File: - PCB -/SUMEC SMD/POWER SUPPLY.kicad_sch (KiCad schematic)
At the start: 14 parts, among them Q3 PMOS, U10 TB6612FNG, U11 LM1084-3.3

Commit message: pcb update cleanup
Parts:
- C?: footprint Connector_JST:JST_SHL_SM06B-SHLS-TF_1x06-1MP_P1.00mm_Horizontal -> Capacitor_SMD:C_1206_3216Metric
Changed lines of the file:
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@@
       (effects (font (size 1.27 1.27)) (justify left))
     )
-    (property "Footprint" "Connector_JST:JST_SHL_SM06B-SHLS-TF_1x06-1MP_P1.00mm_Horizontal" (at 132.3848 119.38 0)
+    (property "Footprint" "Capacitor_SMD:C_1206_3216Metric" (at 132.3848 119.38 0)
       (effects (font (size 1.27 1.27)) hide)
     )

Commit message: pcb schematic update
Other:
- note added: "EXPLANATION"
- note added: "Voltage regulator - 3,3V Output current - 5A"
- note added: "XT-30 Connector (male) Connector with 2mm bullets contacts for currents up to 30 A. Gold-plated contacts Non-interchangeable polarity. connected with XT-30 female type connector that is wired to the battery Battery specs: - 2S LiPo - 3.7V nominal voltage on one cell - 8,4 in total (4,2 fully charged) - 400mAh 1 Bought and 1 Home-made (Terrorist-like)"
- note removed: "XT-30 Connector (male) Connector with 2mm bullets contacts for currents up to 30 A. Gold-plated contacts Non-interchangeable polarity. connected with XT-30 female type connector that is wired to the battery Battery specs: - 3S LiPo - 3.7V nominal voltage on one cell - 12,6 in total (4,2 fully charged) - 400mAh 1 Bought and 1 Home-made (Terrorist-like)"
- note removed: "https://electronics.stackexchange.com/questions/510248/does-tb6612fng-require-additional-circuit-to-control-motor-and-why"
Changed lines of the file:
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@@
     (effects (font (size 1.3 1.3) italic) (justify left bottom))
+  )
+  (text "Voltage regulator - 3,3V\nOutput current - 5A" (at 22.86 100.33 0)
+    (effects (font (size 1.27 1.27)) (justify left bottom))
   )
   (text "H-MŮSTEK" (at 158.75 17.78 0)
     (effects (font (size 1.5 1.5)) (justify left bottom))
   )
-  (text "XT-30 Connector (male)\n\nConnector with 2mm bullets contacts for currents up to 30 A.\nGold-plated contacts\nNon-interchangeable polarity.\nconnected with XT-30 female type connector that is wired to the battery\n\nBattery specs:\n- 3S LiPo\n- 3.7V nominal voltage on one cell\n- 12,6 in total (4,2 fully charged)\n- 400mAh \n\n1 Bought and 1 Home-made (Terrorist-like)"
+  (text "XT-30 Connector (male)\n\nConnector with 2mm bullets contacts for currents up to 30 A.\nGold-plated contacts\nNon-interchangeable polarity.\nconnected with XT-30 female type connector that is wired to the battery\n\nBattery specs:\n- 2S LiPo\n- 3.7V nominal voltage on one cell\n- 8,4 in total (4,2 fully charged)\n- 400mAh \n\n1 Bought and 1 Home-made (Terrorist-like)"
     (at 20.32 177.8 0)
     (effects (font (size 1.27 1.27) italic) (justify left bottom))
@@
   )
   (text "není toho hodně? mohli bysme to ulehčit." (at 199.39 25.4 0)
-    (effects (font (size 2 2)) (justify left bottom))
+    (effects (font (size 2 2) (color 255 0 0 1)) (justify left bottom))
   )
-  (text "https://electronics.stackexchange.com/questions/510248/does-tb6612fng-require-additional-circuit-to-control-motor-and-why"
-    (at 180.34 16.51 0)
-    (effects (font (size 1 1)) (justify left bottom))
+  (text "EXPLANATION" (at 223.52 80.01 0)
+    (effects (font (face "Arial Unicode MS") (size 2 2)) (justify left bottom) (href "https://electronics.stackexchange.com/questions/510248/does-tb6612fng-require-additional-circuit-to-control-motor-and-why"))
   )
   (text "XT30M KONEKTOR" (at 54.61 146.05 0)

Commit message: PCB cooler schematic and start of board making
bettr cal sol
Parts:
- removed C18: 10uF, Capacitor_SMD:C_1206_3216Metric, symbol Device:C_Polarized
- removed C19: 1uF, Capacitor_SMD:C_1206_3216Metric, symbol Device:C_Polarized
- removed C?: 0,1uF, Capacitor_SMD:C_1206_3216Metric, symbol Device:C
- removed C?: 0,5uF, Capacitor_SMD:C_1206_3216Metric, symbol Device:C
- removed C?: 10uF, Capacitor_SMD:C_1206_3216Metric, symbol Device:C
- removed D7: D_Zener, Diode_SMD:D_1206_3216Metric, symbol Device:D_Zener
- removed Q3: PMOS, Package_TO_SOT_THT:TO-220-3_Vertical, symbol Simulation_SPICE:PMOS
- removed R25: 100k, Resistor_SMD:R_1206_3216Metric, symbol Device:R
- removed R26: 1R, Resistor_SMD:R_1206_3216Metric, symbol Device:R
- removed U10: TB6612FNG, Package_SO:SSOP-24_5.3x8.2mm_P0.65mm, symbol Driver_Motor:TB6612FNG
- C? (x2): footprint Capacitor_SMD:C_1206_3216Metric -> Capacitor_THT:CP_Radial_D4.0mm_P2.00mm
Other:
- note added: "Voltage stabilaser LM1084 Input voltage 8,4V Voltage regulator - 3,3V Output current - 5A"
- note removed: "EXPLANATION"
- note removed: "H-MŮSTEK"
- note removed: "Motor Driver - TB6612FNG (IN1 and IN2) can be used to control the motor in one of four function modes: - CW, CCW, short-brake and stop. The two motor outputs (A and B) can be separately controlled, and the speed of each motor is controlled via a PWM input signal with a frequency up to 100kHz. The STBY pin should be pulled high to take the motor out of standby mode. Operating voltage: 2.7-5.5VDC m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"
- note removed: "REFERENCE:"
- note removed: "Voltage regulator - 3,3V Output current - 5A"
- note removed: "není toho hodně? mohli bysme to ulehčit."
- note removed: "p channel enhancement mosfet"
- moved on the sheet: C?, IC?, U11

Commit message: PCB schematic update
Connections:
- net 8V IN renamed VBATT
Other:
- note added: "přidat kondenzatory?"
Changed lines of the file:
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@@
   (junction (at 163.83 41.91) (diameter 0) (color 0 0 0 0)
   )
+  (junction (at 147.32 60.96) (diameter 0) (color 0 0 0 0)
+  )
   (wire (pts (xy 125.73 41.91) (xy 132.08 41.91))
     (stroke (width 0) (type default))
@@
     (stroke (width 0) (type default))
   )
+  (wire (pts (xy 132.08 60.96) (xy 147.32 60.96))
+    (stroke (width 0) (type default))
+  )
   (wire (pts (xy 132.08 41.91) (xy 139.7 41.91))
     (stroke (width 0) (type default))
@@
     (stroke (width 0) (type default))
   )
-  (wire (pts (xy 147.32 49.53) (xy 147.32 62.23))
+  (wire (pts (xy 147.32 49.53) (xy 147.32 60.96))
     (stroke (width 0) (type default))
   )
@@
     (stroke (width 0) (type default))
   )
+  (wire (pts (xy 147.32 60.96) (xy 147.32 62.23))
+    (stroke (width 0) (type default))
+  )
   (wire (pts (xy 170.18 41.91) (xy 163.83 41.91))
     (stroke (width 0) (type default))
@@
   (polyline (pts (xy 82.55 134.62) (xy 193.04 134.62))
     (stroke (width 0) (type default))
+  )
+  (wire (pts (xy 147.32 60.96) (xy 163.83 60.96))
+    (stroke (width 0) (type default))
+  )
+  (text "přidat kondenzatory?" (at 160.02 66.04 0)
+    (effects (font (size 1.27 1.27)) (justify left bottom))
   )
   (text "Voltage stabilaser LM1084\n\nInput voltage 8,4V\nVoltage regulator - 3,3V\nOutput current - 5A"
@@
     (effects (font (size 3 3) bold (color 0 0 0 1)) (justify left bottom))
   )
-  (global_label "8V IN" (shape input) (at 176.53 116.84 0) (fields_autoplaced)
+  (global_label "VBATT" (shape input) (at 176.53 116.84 0) (fields_autoplaced)
     (effects (font (size 1 1) (color 0 0 0 1)) (justify left))
-    (property "Intersheetrefs" "${INTERSHEET_REFS}" (at 182.9131 116.84 0)
+    (property "Intersheetrefs" "${INTERSHEET_REFS}" (at 183.0559 116.84 0)
       (effects (font (size 1.27 1.27)) (justify left) hide)
     )
@@
       (effects (font (size 1.27 1.27)) (justify left))
     )
-    (property "Value" "10uF.stabl" (at 143.51 52.07 0)
+    (property "Value" "10uF.stabl" (at 130.81 54.61 0)
       (effects (font (size 1.27 1.27)) (justify left))
     )
@@
       (effects (font (size 1.27 1.27)) (justify left))
     )
-    (property "Value" "10uF.stabl" (at 176.53 54.61 0)
+    (property "Value" "10uF.stabl" (at 175.26 54.61 0)
       (effects (font (size 1.27 1.27)) (justify left))
     )
@@
     )
   )
-  (symbol (lib_id "power:GND") (at 132.08 60.96 0) (unit 1)
-    (in_bom yes) (on_board yes) (dnp no) (fields_autoplaced)
-    (property "Reference" "#PWR?" (at 132.08 67.31 0)
-      (effects (font (size 1.27 1.27)) hide)
-    )
-    (property "Value" "GND" (at 132.08 66.04 0)
-      (effects (font (size 1.27 1.27)))
-    )
-    (property "Footprint" "" (at 132.08 60.96 0)
-      (effects (font (size 1.27 1.27)) hide)
-    )
-    (property "Datasheet" "" (at 132.08 60.96 0)
-      (effects (font (size 1.27 1.27)) hide)
-    )
-    (pin "1")
-    (instances
-      (project "sumec"
-        (path "/fc70a1a8-ed7c-4a0f-9b1a-f23293528385"
-          (reference "#PWR?") (unit 1)
-        )
-        (path "/fc70a1a8-ed7c-4a0f-9b1a-f23293528385/2febd48c-c6ec-477b-ac64-6fa98a41fff0"
-          (reference "#PWR043") (unit 1)
-        )
-      )
-    )
-  )
   (symbol (lib_id "power:GND") (at 182.88 119.38 90) (unit 1)
     (in_bom yes) (on_board yes) (dnp no)
@@
         )
       )
-    )
-  )
-  (symbol (lib_id "power:GND") (at 163.83 60.96 0) (unit 1)
-    (in_bom yes) (on_board yes) (dnp no) (fields_autoplaced)
-    (property "Reference" "#PWR?" (at 163.83 67.31 0)
-      (effects (font (size 1.27 1.27)) hide)
-    )
-    (property "Value" "GND" (at 163.83 66.04 0)
-      (effects (font (size 1.27 1.27)))
-    )
-    (property "Footprint" "" (at 163.83 60.96 0)
-      (effects (font (size 1.27 1.27)) hide)
-    )
-    (property "Datasheet" "" (at 163.83 60.96 0)
-      (effects (font (size 1.27 1.27)) hide)
-    )
-    (pin "1")
-    (instances
-      (project "sumec"
-        (path "/fc70a1a8-ed7c-4a0f-9b1a-f23293528385"
-          (reference "#PWR?") (unit 1)
-        )
-        (path "/fc70a1a8-ed7c-4a0f-9b1a-f23293528385/2febd48c-c6ec-477b-ac64-6fa98a41fff0"
-          (reference "#PWR045") (unit 1)
-        )
-      )

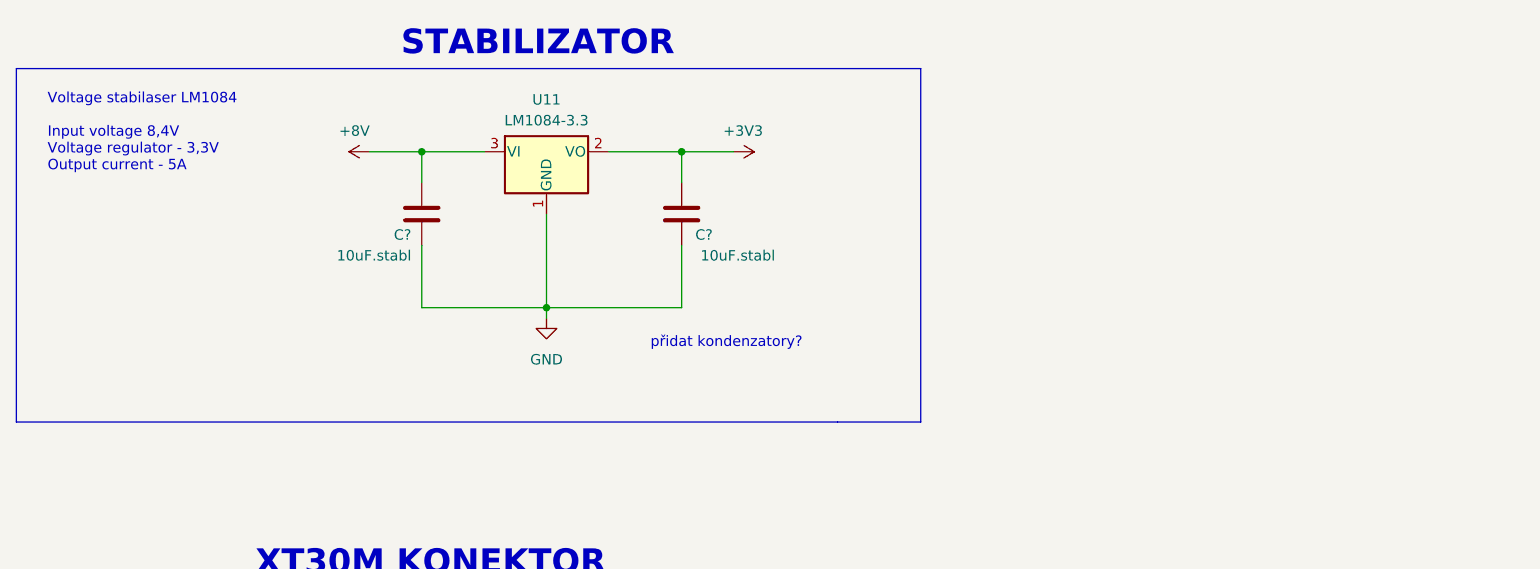
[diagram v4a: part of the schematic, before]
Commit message: Added 5V regulator
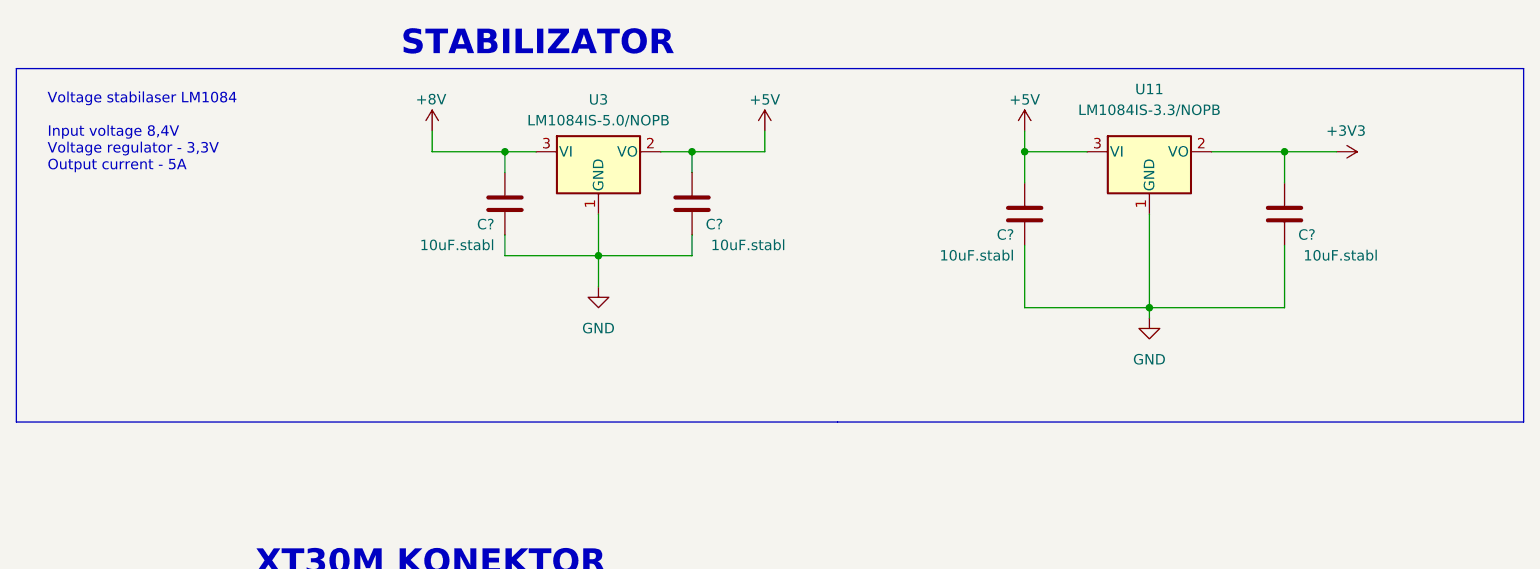
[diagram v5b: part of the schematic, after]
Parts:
- added C? (x2): 10uF.stabl, Capacitor_SMD:C_1206_3216Metric_Pad1.33x1.80mm_HandSolder, symbol Device:C
- added U3: LM1084IS-5.0/NOPB, Package_TO_SOT_SMD:TO-252-3_TabPin2, symbol Regulator_Linear:LM1084-3.3
- C? (x2): footprint Capacitor_THT:CP_Radial_D4.0mm_P2.00mm -> Capacitor_SMD:C_1206_3216Metric_Pad1.33x1.80mm_HandSolder
- U11: value LM1084-3.3 -> LM1084IS-3.3/NOPB; footprint Package_TO_SOT_THT:TO-220-3_Vertical -> Package_TO_SOT_SMD:TO-252-3_TabPin2
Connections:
- net +8V: now also C?.1, U3.3 (VI); no longer C?.1, U11.3 (VI)
- net GND: now also C?.2, C?.2, U3.1 (GND)
- new net +5V: C?.1, C?.1, U11.3 (VI), U3.2 (VO)
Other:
- note removed: "přidat kondenzatory?"
- moved on the sheet: C?, U11

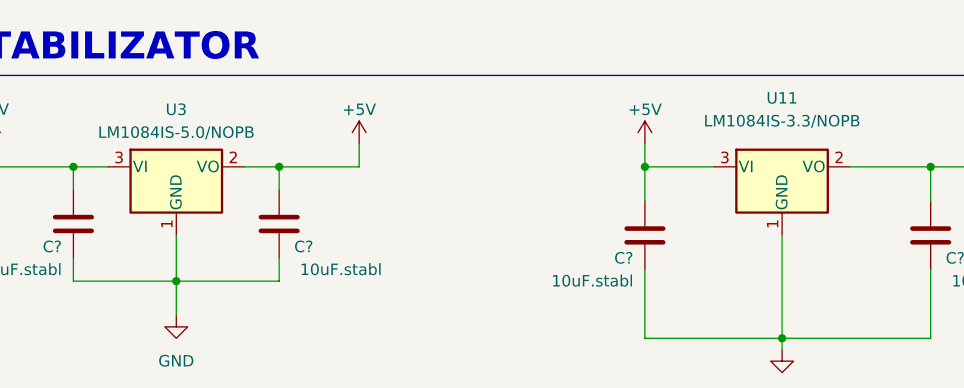
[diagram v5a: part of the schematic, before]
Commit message: Main switch changed, USB parts rearranged
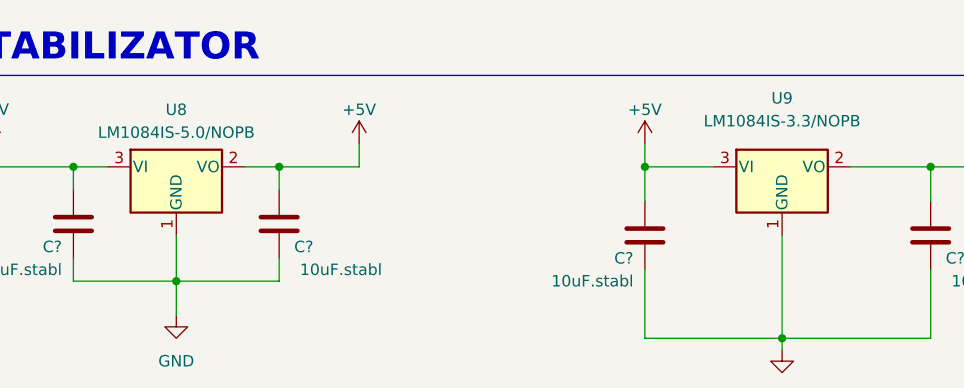
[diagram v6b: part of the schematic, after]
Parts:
- renumbered U3 to U8, U11 to U9
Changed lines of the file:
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@@
         )
         (path "/fc70a1a8-ed7c-4a0f-9b1a-f23293528385/2febd48c-c6ec-477b-ac64-6fa98a41fff0"
-          (reference "#PWR028") (unit 1)
+          (reference "#PWR047") (unit 1)
         )
       )
@@
   (symbol (lib_id "power:+5V") (at 205.74 39.37 0) (unit 1)
     (in_bom yes) (on_board yes) (dnp no) (fields_autoplaced)
-    (property "Reference" "#PWR022" (at 205.74 43.18 0)
+    (property "Reference" "#PWR045" (at 205.74 43.18 0)
       (effects (font (size 1.27 1.27)) hide)
     )
@@
       (project "sumec"
         (path "/fc70a1a8-ed7c-4a0f-9b1a-f23293528385/2febd48c-c6ec-477b-ac64-6fa98a41fff0"
-          (reference "#PWR022") (unit 1)
+          (reference "#PWR045") (unit 1)
         )
       )
@@
         )
         (path "/fc70a1a8-ed7c-4a0f-9b1a-f23293528385/2febd48c-c6ec-477b-ac64-6fa98a41fff0"
-          (reference "C1") (unit 1)
+          (reference "C12") (unit 1)
         )
       )
@@
   (symbol (lib_id "Regulator_Linear:LM1084-3.3") (at 220.98 41.91 0) (unit 1)
     (in_bom yes) (on_board yes) (dnp no) (fields_autoplaced)
-    (property "Reference" "U11" (at 220.98 34.29 0)
+    (property "Reference" "U9" (at 220.98 34.29 0)
       (effects (font (size 1.27 1.27)))
     )
@@
       (project "sumec"
         (path "/fc70a1a8-ed7c-4a0f-9b1a-f23293528385/2febd48c-c6ec-477b-ac64-6fa98a41fff0"
-          (reference "U11") (unit 1)
+          (reference "U9") (unit 1)
         )
       )
@@
         )
         (path "/fc70a1a8-ed7c-4a0f-9b1a-f23293528385/2febd48c-c6ec-477b-ac64-6fa98a41fff0"
-          (reference "C2") (unit 1)
+          (reference "C13") (unit 1)
         )
       )
@@
         )
         (path "/fc70a1a8-ed7c-4a0f-9b1a-f23293528385/2febd48c-c6ec-477b-ac64-6fa98a41fff0"
-          (reference "#PWR030") (unit 1)
+          (reference "#PWR046") (unit 1)
         )
       )
@@
   (symbol (lib_id "Regulator_Linear:LM1084-3.3") (at 153.67 41.91 0) (unit 1)
     (in_bom yes) (on_board yes) (dnp no) (fields_autoplaced)
-    (property "Reference" "U3" (at 153.67 35.56 0)
+    (property "Reference" "U8" (at 153.67 35.56 0)
       (effects (font (size 1.27 1.27)))
     )
@@
       (project "sumec"
         (path "/fc70a1a8-ed7c-4a0f-9b1a-f23293528385/2febd48c-c6ec-477b-ac64-6fa98a41fff0"
-          (reference "U3") (unit 1)
+          (reference "U8") (unit 1)
         )
       )
@@
         )
         (path "/fc70a1a8-ed7c-4a0f-9b1a-f23293528385/2febd48c-c6ec-477b-ac64-6fa98a41fff0"
-          (reference "#PWR016") (unit 1)
+          (reference "#PWR042") (unit 1)
         )
       )
@@
         )
         (path "/fc70a1a8-ed7c-4a0f-9b1a-f23293528385/2febd48c-c6ec-477b-ac64-6fa98a41fff0"
-          (reference "#PWR029") (unit 1)
+          (reference "#PWR044") (unit 1)
         )
       )
@@
   (symbol (lib_id "power:+8V") (at 133.35 39.37 0) (unit 1)
     (in_bom yes) (on_board yes) (dnp no)
-    (property "Reference" "#PWR024" (at 133.35 43.18 0)
+    (property "Reference" "#PWR041" (at 133.35 43.18 0)
       (effects (font (size 1.27 1.27)) hide)
     )
@@
       (project "sumec"
         (path "/fc70a1a8-ed7c-4a0f-9b1a-f23293528385/2febd48c-c6ec-477b-ac64-6fa98a41fff0"
-          (reference "#PWR024") (unit 1)
+          (reference "#PWR041") (unit 1)
         )
       )
@@
   (symbol (lib_id "power:+5V") (at 173.99 39.37 0) (unit 1)
     (in_bom yes) (on_board yes) (dnp no) (fields_autoplaced)
-    (property "Reference" "#PWR017" (at 173.99 43.18 0)
+    (property "Reference" "#PWR043" (at 173.99 43.18 0)
       (effects (font (size 1.27 1.27)) hide)
     )
@@
       (project "sumec"
         (path "/fc70a1a8-ed7c-4a0f-9b1a-f23293528385/2febd48c-c6ec-477b-ac64-6fa98a41fff0"
-          (reference "#PWR017") (unit 1)
-        )
-      )
+          (reference "#PWR043") (unit 1)
+        )
+      )
